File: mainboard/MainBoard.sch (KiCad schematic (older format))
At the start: 38 parts, among them J1 CONN_1x4, J2 CONN_2X3, J3 CONN_2X3, J5 SWDEBUG_CONNECTOR, J7 CONN_2X12, U1 VX07805-1000, U2 TPS2115A, U3 ld1117s33

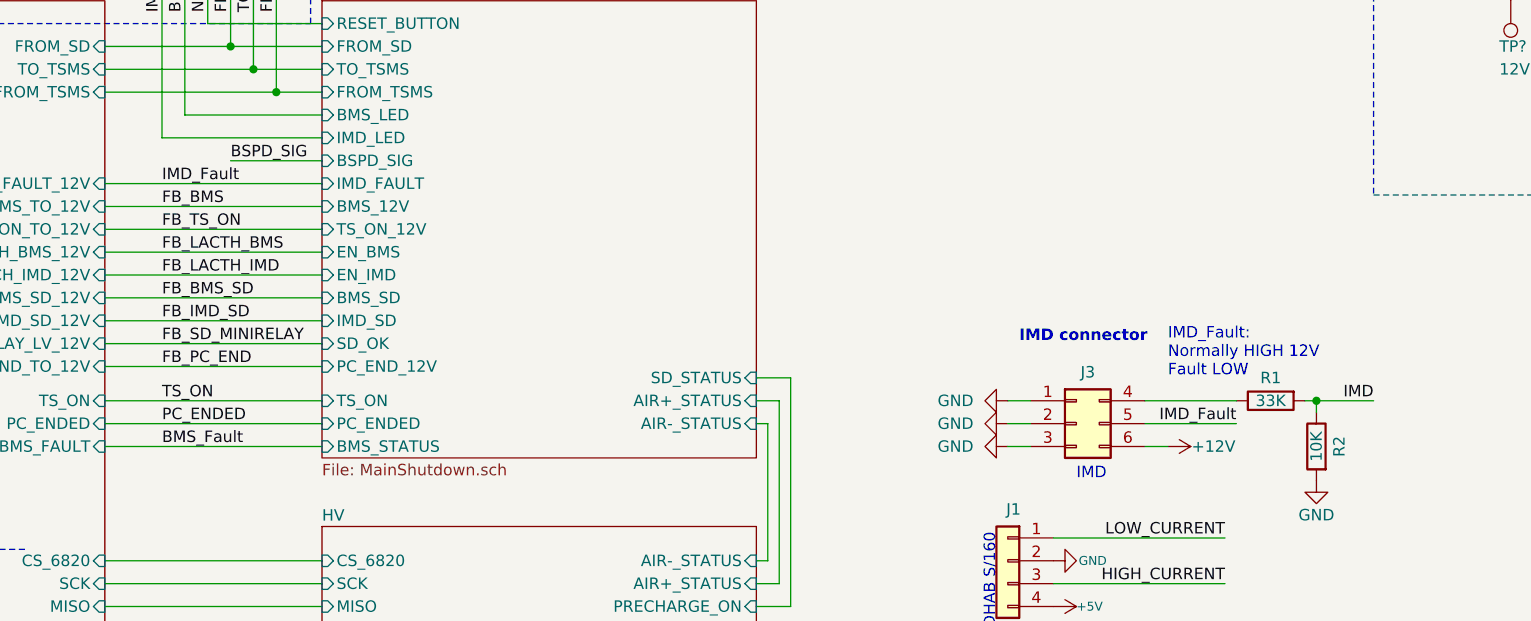
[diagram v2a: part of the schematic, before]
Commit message: renamed shutdown nets
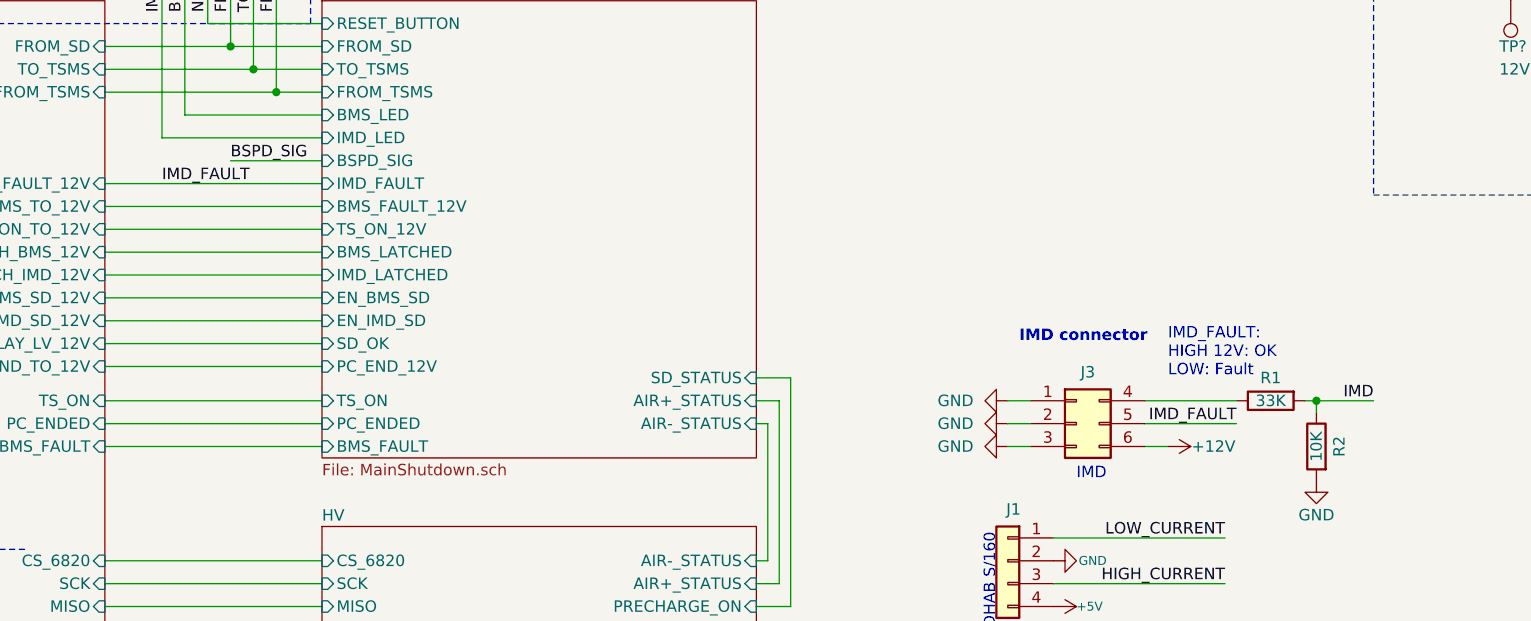
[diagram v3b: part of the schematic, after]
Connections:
- net IMD_Fault renamed IMD_FAULT
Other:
- note added: "IMD_FAULT:\nHIGH 12V: OK\nLOW: Fault"
- note removed: "IMD_Fault:\nNormally HIGH 12V\nFault LOW"
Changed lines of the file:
@@
 Comment4 ""
 $EndDescr
-Text Label 3400 5300 0    50   ~ 0
-BMS_Fault
-Text Label 3400 5100 0    50   ~ 0
-TS_ON
-Text Label 3400 5200 0    50   ~ 0
-PC_ENDED
 $Comp
 L power:GND #PWR07
@@
 $EndComp
 Text Label 8100 5200 2    50   ~ 0
-IMD_Fault
+IMD_FAULT
 $Comp
 L power:GND #PWR010
@@
 Wire Wire Line
 	4100 3950 3400 3950
-Text Label 3400 4850 0    50   ~ 0
-FB_SD_MINIRELAY
 Wire Wire Line
 	6000 5000 6150 5000
@@
 Wire Wire Line
 	3150 4350 4100 4350
-Text Label 3400 4350 0    50   ~ 0
-FB_TS_ON
-Text Label 3400 4450 0    50   ~ 0
-FB_LACTH_BMS
-Text Label 3400 4550 0    50   ~ 0
-FB_LACTH_IMD
-Text Label 3400 4650 0    50   ~ 0
-FB_BMS_SD
-Text Label 3400 4750 0    50   ~ 0
-FB_IMD_SD
-Text Label 3400 4950 0    50   ~ 0
-FB_PC_END
 Text Label 3400 7000 0    50   ~ 0
 FB_TS_OVER_60V
@@
 F2 "PC_ENDED" I L 4100 5200 50
 F3 "TS_ON" I L 4100 5100 50
-F4 "BMS_STATUS" I L 4100 5300 50
-F5 "FROM_SD" I L 4100 3550 50
-F6 "RESET_BUTTON" I L 4100 3450 50
-F7 "TO_TSMS" I L 4100 3650 50
-F8 "FROM_TSMS" I L 4100 3750 50
-F9 "IMD_LED" I L 4100 3950 50
-F10 "BMS_LED" I L 4100 3850 50
-F11 "AIR+_STATUS" I R 6000 5100 50
-F12 "AIR-_STATUS" I R 6000 5200 50
-F13 "SD_STATUS" I R 6000 5000 50
-F14 "IMD_FAULT" I L 4100 4150 50
-F15 "SD_OK" I L 4100 4850 50
-F16 "TS_ON_12V" I L 4100 4350 50
-F17 "EN_BMS" I L 4100 4450 50
-F18 "EN_IMD" I L 4100 4550 50
-F19 "IMD_SD" I L 4100 4750 50
-F20 "BMS_SD" I L 4100 4650 50
-F21 "PC_END_12V" I L 4100 4950 50
-F22 "BMS_12V" I L 4100 4250 50
-F23 "BSPD_SIG" I L 4100 4050 50
+F4 "FROM_SD" I L 4100 3550 50
+F5 "RESET_BUTTON" I L 4100 3450 50
+F6 "TO_TSMS" I L 4100 3650 50
+F7 "FROM_TSMS" I L 4100 3750 50
+F8 "IMD_LED" I L 4100 3950 50
+F9 "BMS_LED" I L 4100 3850 50
+F10 "AIR+_STATUS" I R 6000 5100 50
+F11 "AIR-_STATUS" I R 6000 5200 50
+F12 "SD_STATUS" I R 6000 5000 50
+F13 "IMD_FAULT" I L 4100 4150 50
+F14 "SD_OK" I L 4100 4850 50
+F15 "TS_ON_12V" I L 4100 4350 50
+F16 "PC_END_12V" I L 4100 4950 50
+F17 "BSPD_SIG" I L 4100 4050 50
+F18 "EN_IMD_SD" I L 4100 4750 50
+F19 "EN_BMS_SD" I L 4100 4650 50
+F20 "BMS_LATCHED" I L 4100 4450 50
+F21 "IMD_LATCHED" I L 4100 4550 50
+F22 "BMS_FAULT" I L 4100 5300 50
+F23 "BMS_FAULT_12V" I L 4100 4250 50
 $EndSheet
-Text Label 3400 4250 0    50   ~ 0
-FB_BMS
 Wire Wire Line
 	4100 4250 3150 4250
 Text Label 3400 4150 0    50   ~ 0
-IMD_Fault
+IMD_FAULT
 Wire Wire Line
 	4100 4150 3150 4150
@@
 $EndSheet
 Text Notes 7800 5000 0    50   ~ 0
-IMD_Fault:\nNormally HIGH 12V\nFault LOW
+IMD_FAULT:\nHIGH 12V: OK\nLOW: Fault
 Text Label 5000 2100 0    50   ~ 0
 FROM_SD
